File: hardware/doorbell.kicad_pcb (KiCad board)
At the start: 2 copper layers, 47 x 70 mm, 16 parts, among them J1 CONN_01X02, J2 CONN_01X09, J3 CONN_01X07, P1 DOOR, P2 STRIP_CONN, Q1 MMBT3904, U1 LD1117S33CTR, U2 4N25, U3 ESP-12

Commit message: Fix some library issues
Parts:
- P1: value DOOR -> DOOR_CONN
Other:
- net class Default: trace_width 0.25 -> 0.4

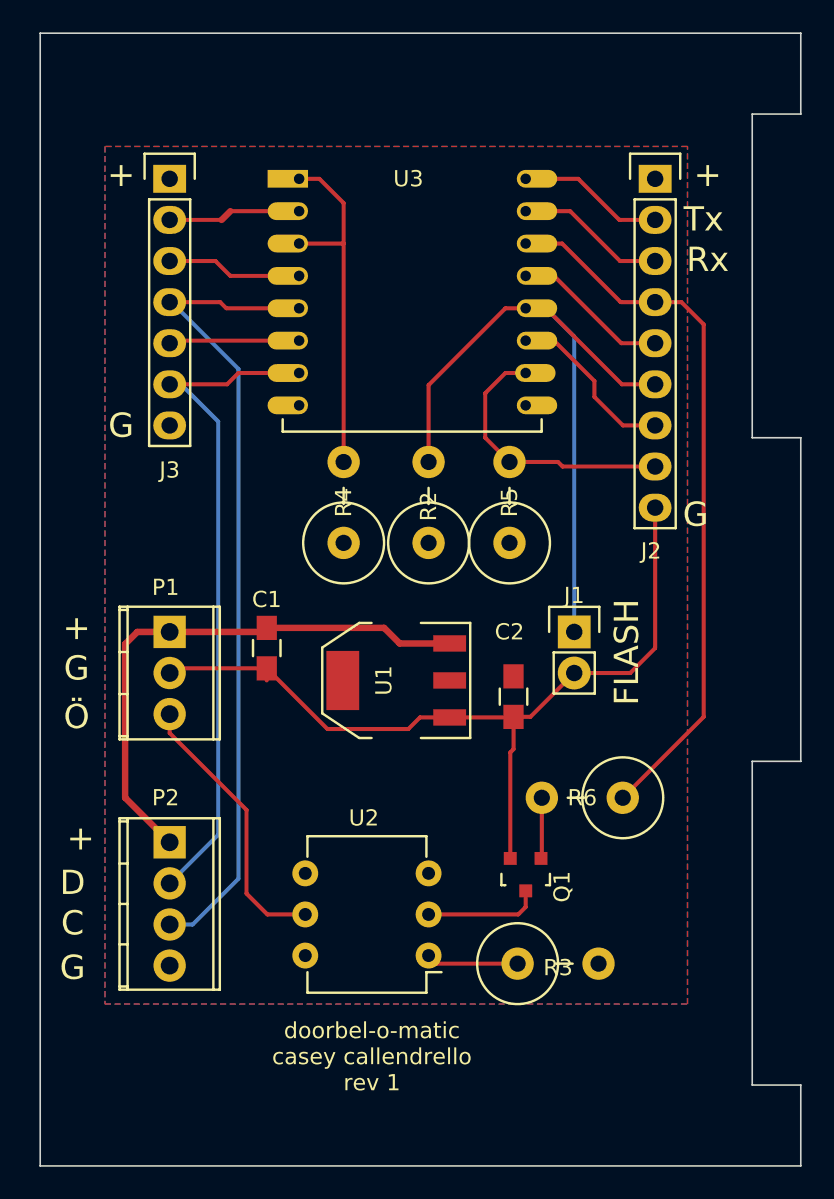
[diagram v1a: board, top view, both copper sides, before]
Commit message: Fix trace width, expand copper fills
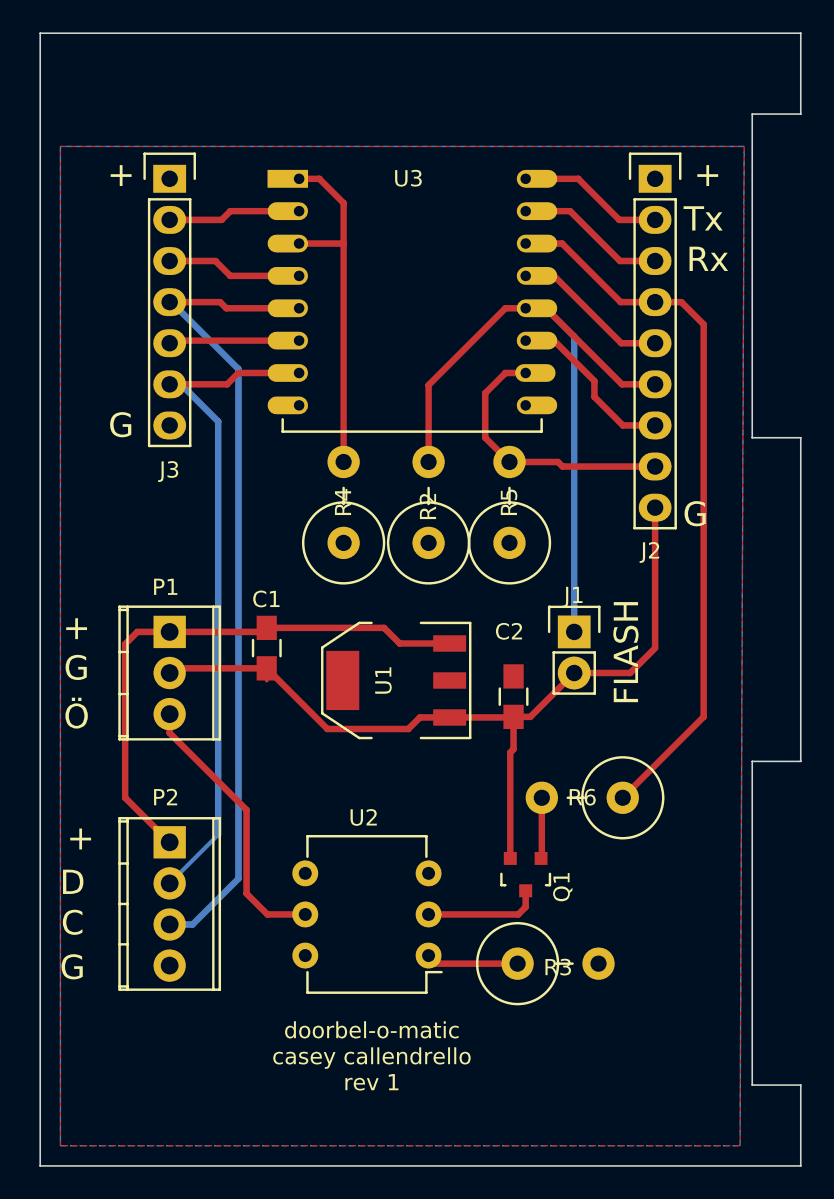
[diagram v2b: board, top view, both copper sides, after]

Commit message: Shrink board, expand copper, change Q1 bom
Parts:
- Q1: value MMBT3904 -> BC_846B
- moved R3 7.45 mm to (86.8, 101.8)
- moved U2 5.00 mm to (74.2, 102.0)
- moved Q1 4.62 mm to (81.4, 97.6)
- moved R6 3.98 mm to (85.8, 94.0)
- moved P2 3.80 mm to (58.0, 96.2)
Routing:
- net Net-(R3-Pad1): track 5.71 -> 10.2 mm
- net D5: track 46.1 -> 41.7 mm
- net GND: track 52.0 -> 48.0 mm
- net LOCK: track 17.2 -> 13.9 mm
- net Net-(Q1-Pad1): track 3.77 -> 2.99 mm
- net CLK: track 51.0 -> 51.7 mm
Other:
- board size 47 x 70 mm -> 47 x 57 mm
- net class Default: via_dia 0.6 -> 0.7
- net class power: via_dia 0.6 -> 0.6858
- rule via_min_drill: 0.3 -> 0.3302
- rule via_min_size: 0.4 -> 0.6858

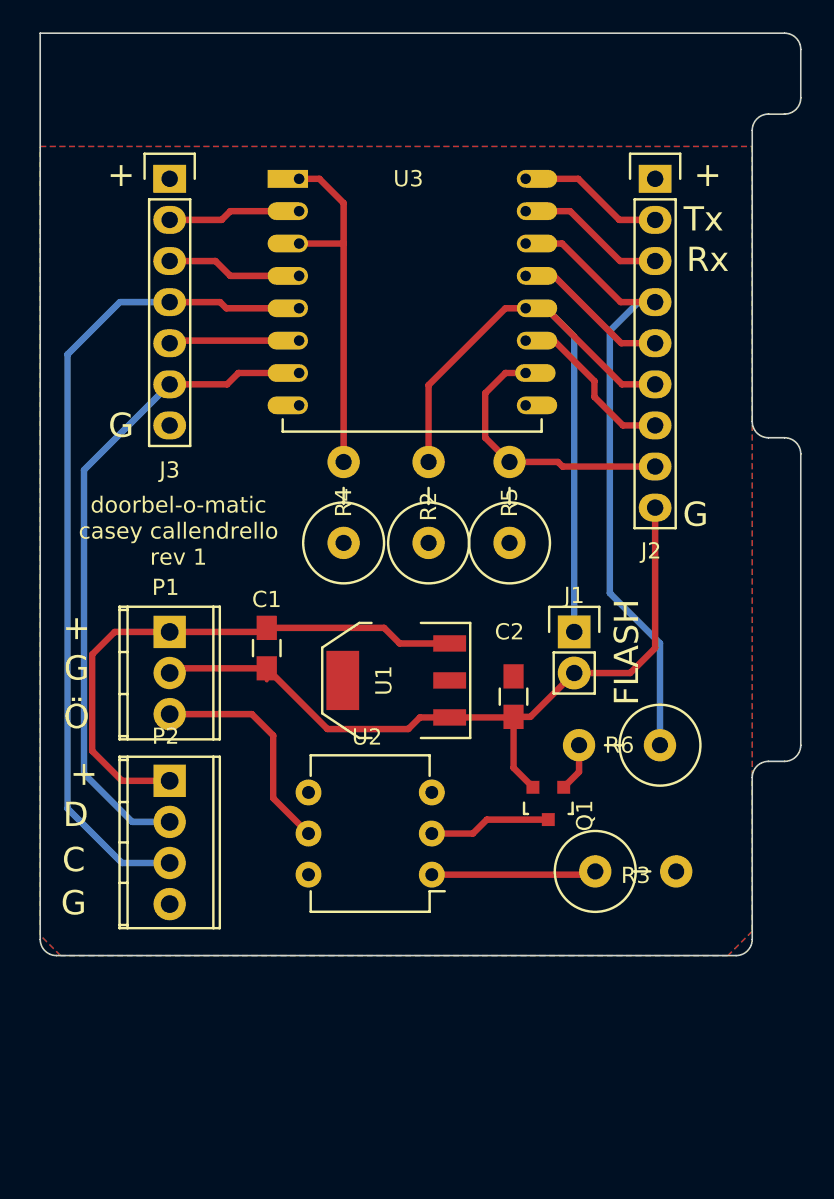
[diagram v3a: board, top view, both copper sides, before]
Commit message: Convert to include a switching voltage regulator breakout
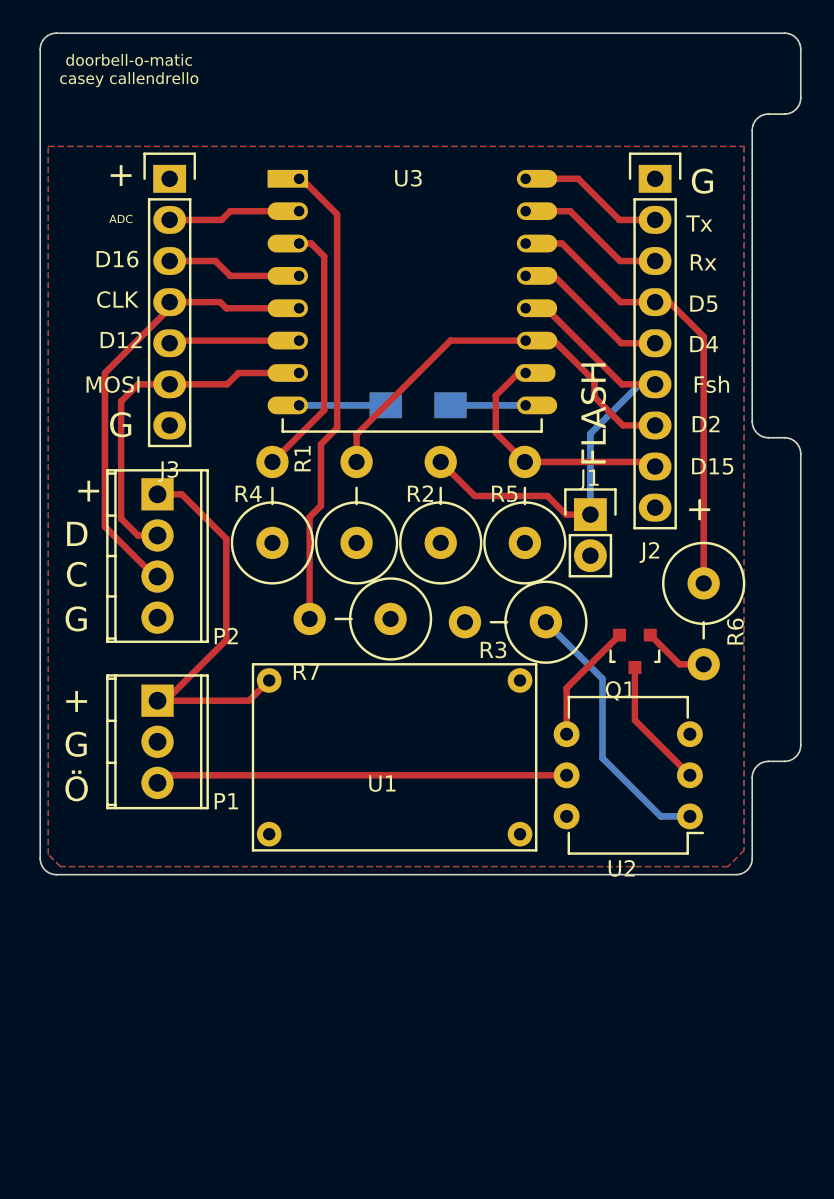
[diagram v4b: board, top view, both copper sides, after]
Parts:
- removed C2: 10µF, Capacitors_SMD:C_0805_HandSoldering
- added R1: 10K, Resistors_ThroughHole:Resistor_Vertical_RM5mm, F.Cu at (69.5, 79.0)
- added R7: 10K, Resistors_ThroughHole:Resistor_Vertical_RM5mm, F.Cu at (69.2, 86.2)
- added REF**: Symbol_OSHW-Logo_SilkScreen, Symbols:Symbol_OSHW-Logo_SilkScreen, B.Cu at (71.5, 94.0)
- C1: value 100nF -> 0.1µF; footprint Capacitors_SMD:C_0805_HandSoldering -> Capacitors_SMD:C_1206_HandSoldering; moved to B.Cu
- U1: value LD1117S33CTR -> MP2307_Breakout; footprint TO_SOT_Packages_SMD:SOT-223 -> Doorbell:MP2307_Breakout
- moved P2 17.7 mm to (57.2, 78.5)
- moved C1 17.7 mm to (73.3, 73.0), turned to 0 degrees
- moved R3 17.4 mm to (78.8, 86.4), turned to 180 degrees
- moved U2 16.4 mm to (90.2, 98.4)
- moved Q1 10.8 mm to (86.8, 88.2)
- moved R6 9.13 mm to (91.0, 86.5), turned to 270 degrees
- moved U1 7.85 mm to (64.2, 90.0), turned to 0 degrees
- moved J1 7.32 mm to (84.0, 79.8)
- moved R4 4.40 mm to (64.3, 79.0)
- moved P1 4.32 mm to (57.2, 91.2)
- moved R5 0.95 mm to (80.0, 79.0)
- moved R2 0.75 mm to (74.8, 79.0)
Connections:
- C1 pad 1: VIN -> +3V3
- J2 pad 1: +3V3 -> GND
- J2 pad 9: GND -> +3V3
- U1 pad 1: GND -> VIN
- U1 pad 2: +3V3 -> GND
- U1 pad 3: VIN -> +3V3
- U1 pad 4: (no net) -> GND
- U3 pad 1: Net-(R4-Pad2) -> Net-(R7-Pad2)
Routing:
- net GND: track 48.0 -> 12.1 mm
- net Net-(R7-Pad2): track 0.00 -> 29.0 mm
- net CLK: track 51.7 -> 28.3 mm
- net MOSI: track 41.8 -> 22.4 mm
- net D2: track 10.7 -> 25.3 mm
- net LOCK: track 13.9 -> 26.1 mm
- net D5: track 41.7 -> 30.4 mm
- net FLASH: track 44.6 -> 33.4 mm
- net VIN: track 34.7 -> 24.9 mm
- net Net-(R3-Pad1): track 10.2 -> 17.1 mm
- net Net-(R4-Pad2): track 22.1 -> 15.9 mm
- net +3V3: track 0.00 -> 5.35 mm
- net D15: track 17.0 -> 15.4 mm
- net Net-(Q1-Pad1): track 2.99 -> 4.05 mm
- net Net-(Q1-Pad3): track 7.56 -> 8.07 mm
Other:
- board size 47 x 57 mm -> 47 x 52 mm
- board text added: "ADC"
- board text added: "CLK"
- board text added: "D12"
- board text added: "D15"
- board text added: "D16"
- board text added: "D2"
- board text added: "D4"
- board text added: "D5"
- board text added: "Fsh"
- board text added: "MOSI"
- board text added: "doorbell-o-matic casey callendrello"
- board text added: "github.com/squeed/esp-doorbell"
- board text added: "it's open sores"
- board text removed: "doorbel-o-matic casey callendrello rev 1"

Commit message: Add Vin decoupling cap
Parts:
- added C2: 0.1µF, Capacitors_SMD:C_1206_HandSoldering, B.Cu at (64.0, 94.8)
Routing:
- net VIN: track 24.9 -> 27.7 mm
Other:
- board text removed: "it's open sores"
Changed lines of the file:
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@@
 (kicad_pcb (version 4) (host pcbnew 4.0.2-stable)
   (general
-    (links 47)
+    (links 49)
     (no_connects 0)
     (area 49.949999 49.949999 97.050001 102.050001)
     (thickness 1.6)
     (drawings 47)
-    (tracks 103)
+    (tracks 105)
     (zones 0)
-    (modules 18)
+    (modules 19)
     (nets 23)
   )
   (page A4)
   (layers
-    (0 Top signal)
+    (0 Top signal hide)
     (31 Bottom signal)
     (34 B.Paste user)
     (35 F.Paste user)
-    (36 B.SilkS user)
+    (36 B.SilkS user hide)
     (37 F.SilkS user)
     (38 B.Mask user)
@@
       (net 22 "Net-(R7-Pad2)"))
   )
-  (gr_text "it's open sores" (at 71.75 99.25) (layer B.SilkS)
+  (module Capacitors_SMD:C_1206_HandSoldering (layer Bottom)
+    (at 64 94.75 90)
+    (descr "Capacitor SMD 1206, hand soldering")
+    (tags "capacitor 1206")
+    (attr smd)
+    (fp_text reference C2 (at 0 2.3 90) (layer B.SilkS)
+      (effects (font (size 1 1) (thickness 0.15)) (justify mirror))
+    )
+    (fp_text value 0.1µF (at 0 -2.3 90) (layer B.Fab)
+      (effects (font (size 1 1) (thickness 0.15)) (justify mirror))
+    )
+    (fp_line (start -3.3 1.15) (end 3.3 1.15) (layer B.CrtYd) (width 0.05))
+    (fp_line (start -3.3 -1.15) (end 3.3 -1.15) (layer B.CrtYd) (width 0.05))
+    (fp_line (start -3.3 1.15) (end -3.3 -1.15) (layer B.CrtYd) (width 0.05))
+    (fp_line (start 3.3 1.15) (end 3.3 -1.15) (layer B.CrtYd) (width 0.05))
+    (fp_line (start 1 1.025) (end -1 1.025) (layer B.SilkS) (width 0.15))
+    (fp_line (start -1 -1.025) (end 1 -1.025) (layer B.SilkS) (width 0.15))
+    (pad 1 smd rect (at -2 0 90) (size 2 1.6) (layers Bottom B.Paste B.Mask)
+      (net 2 GND))
+    (pad 2 smd rect (at 2 0 90) (size 2 1.6) (layers Bottom B.Paste B.Mask)
+      (net 1 VIN))
+    (model Capacitors_SMD.3dshapes/C_1206_HandSoldering.wrl
+      (at (xyz 0 0 0))
+      (scale (xyz 1 1 1))
+      (rotate (xyz 0 0 0))
+    )
+  )
+  (gr_text "\n\n" (at 71.75 99.25) (layer B.SilkS)
     (effects (font (size 1 1) (thickness 0.2)) (justify mirror))
   )
@@
   (gr_line (start 97 51) (end 97 54) (angle 90) (layer Edge.Cuts) (width 0.1))
   (gr_line (start 51 50) (end 96 50) (angle 90) (layer Edge.Cuts) (width 0.1))
+  (segment (start 64.15 90) (end 64.15 92.6) (width 0.4) (layer Bottom) (net 1) (status C00000))
+  (segment (start 64.15 92.6) (end 64 92.75) (width 0.4) (layer Bottom) (net 1) (status C00000))
   (segment (start 57.25 91.25) (end 62.9 91.25) (width 0.4) (layer Top) (net 1) (status 10))
   (segment (start 62.9 91.25) (end 64.15 90) (width 0.4) (layer Top) (net 1) (status 20))
